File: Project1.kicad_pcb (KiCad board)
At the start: 2 copper layers, 18.3 x 13.7 mm, 16 parts, among them J1 48037-0001, U1 MCP1702T-3302E/CB, U2 MCP6022T-I/ST

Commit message: Add report and necessary files
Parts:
- moved C4 0.28 mm to (36.0, 20.8)
- moved C1 0.08 mm to (36.0, 22.3)
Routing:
- net /VOUT_REG: track 11.5 -> 12.6 mm
- net /PWR_USB: track 5.54 -> 6.09 mm

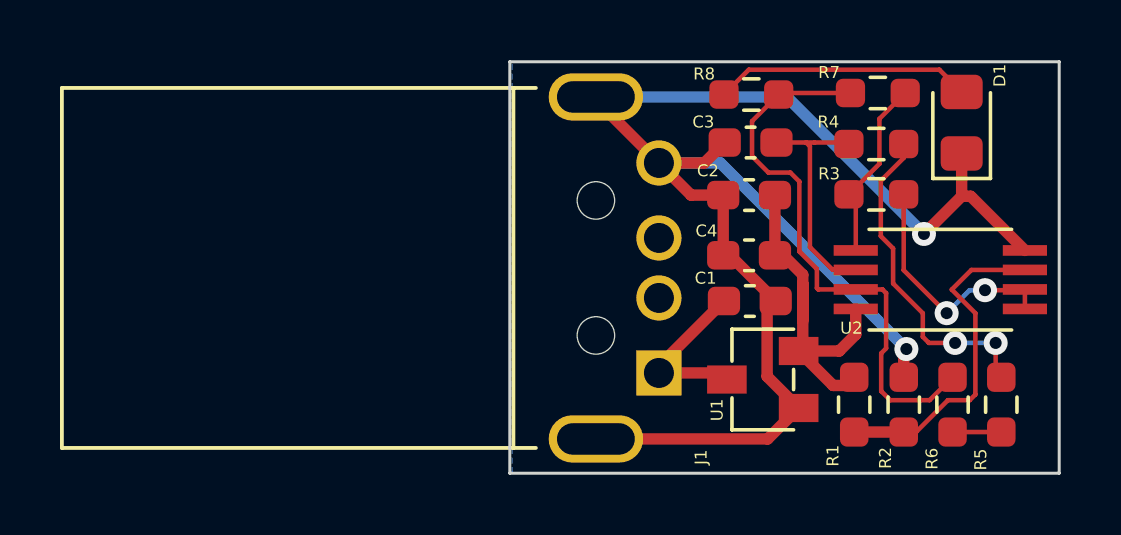
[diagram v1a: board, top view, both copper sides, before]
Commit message: Fix trace errors in pcb
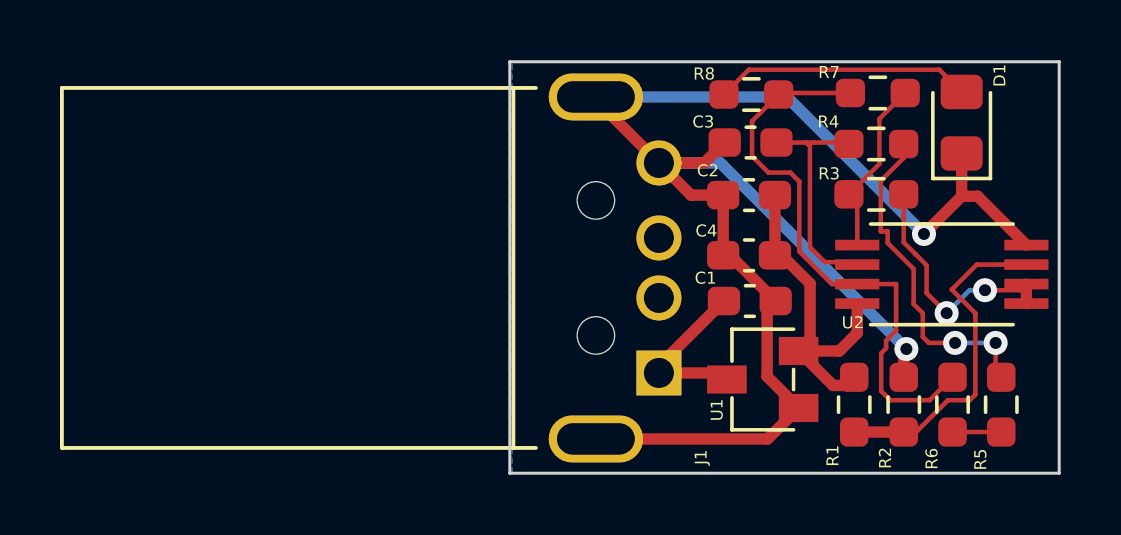
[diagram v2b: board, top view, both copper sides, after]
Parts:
- moved U2 0.18 mm to (42.4, 21.4)
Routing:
- net /VOUT_REG: track 12.6 -> 11.9 mm
